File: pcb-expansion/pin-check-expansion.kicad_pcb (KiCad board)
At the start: 2 copper layers, 38.1 x 53.3 mm, 25 parts, among them J1 Conn_01x04, SW1 MX-NoLED, SW2 MX-NoLED, U1 MCP23008-xP

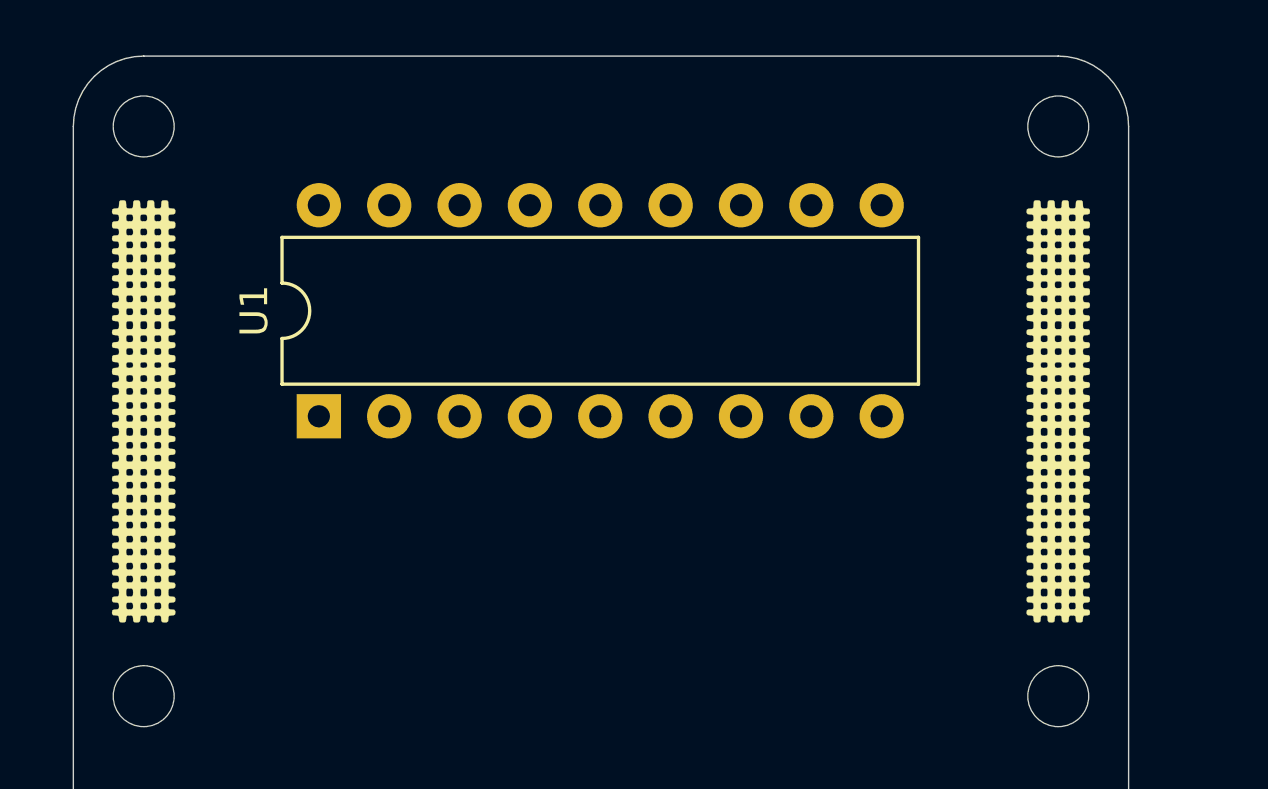
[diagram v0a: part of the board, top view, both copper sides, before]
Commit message: start updating expansion board to use mcp23017
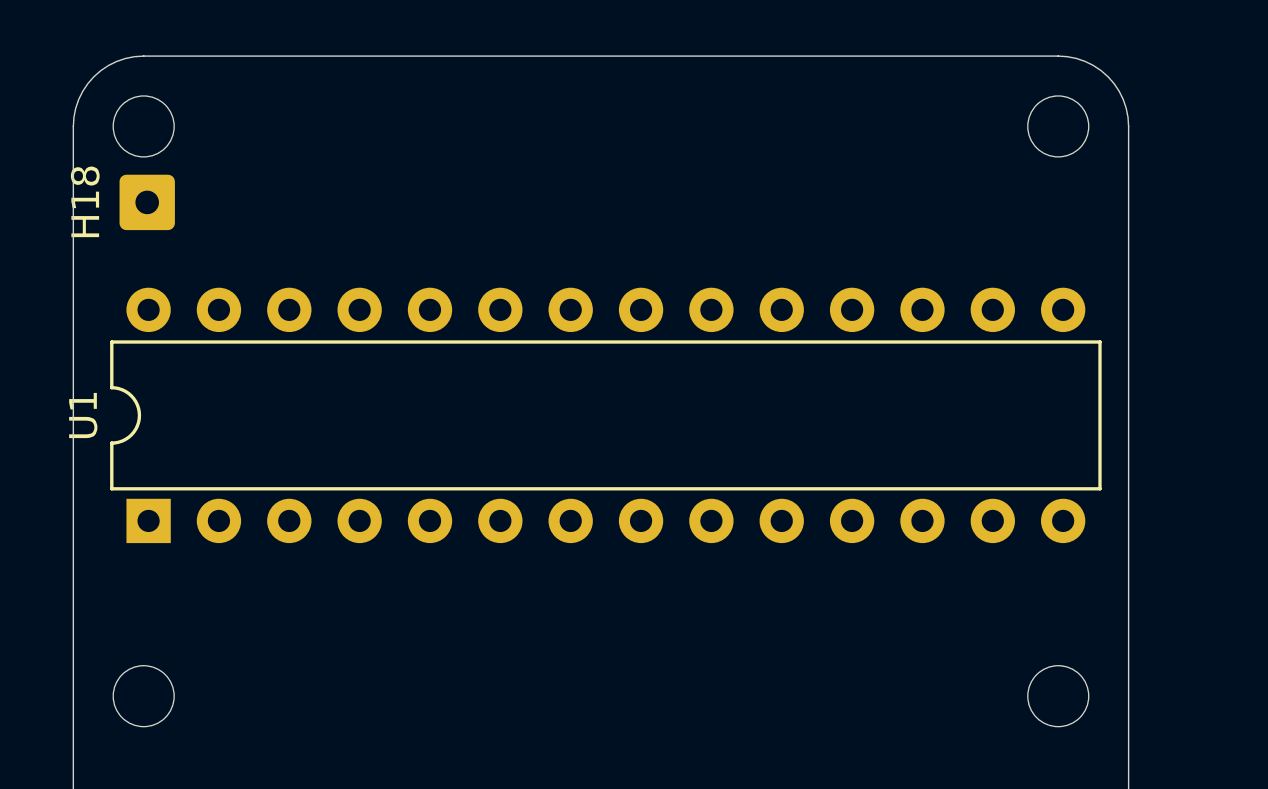
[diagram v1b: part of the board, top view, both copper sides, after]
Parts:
- removed G*** (x2): LOGO, pin-check-expansion.pretty:pin-check-pattern
- added H18: MountingHole_Pad, Connector_Wire:SolderWire-0.25sqmm_1x01_D0.65mm_OD2mm, F.Cu at (158.9, 86.1)
- U1: value MCP23008-xP -> MCP23017_SP; footprint Package_DIP:DIP-18_W7.62mm -> Package_DIP:DIP-28_W7.62mm
- moved U1 7.22 mm to (158.9, 97.6)
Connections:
- net Net-(U1-Pad7) renamed /GPB6
- net Net-(U1-Pad8) renamed /GPB7
- U1 pad 1: /SCL -> /GPB0
- U1 pad 10: /ColE -> GND
- U1 pad 11: /ColF -> Net-(U1-Pad11)
- U1 pad 12: /GP2 -> /SCL
- U1 pad 13: /GP3 -> /SDA
- U1 pad 14: /GP4 -> Net-(U1-Pad14)
- U1 pad 15: /GP5 -> GND
- U1 pad 16: /GP6 -> GND
- U1 pad 17: /GP7 -> GND
- U1 pad 2: /SDA -> /GPB1
- U1 pad 3: GND -> /GPB2
- U1 pad 4: GND -> /GPB3
- U1 pad 5: GND -> /GPB4
- U1 pad 6: +5V -> /GPB5
- U1 pad 9: GND -> +5V
